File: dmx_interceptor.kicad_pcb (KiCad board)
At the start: 4 copper layers, 86 x 53 mm, 8 parts, among them J1 TB010-508-02BE, J2 TB010-508-02BE, J3 TB004-508-03BE, J4 TB004-508-03BE, U1 ARDUINO_PRO_MINI

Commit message: output files for ordering & pcb fix
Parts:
- R1: footprint mart_library:smd_0603_1608-Metric -> dmx_interceptor:smd_0603_1608-Metric
- mod1, mod2: footprint mart_library:max485_to_rs485 -> dmx_interceptor:max485_to_rs485
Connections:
- U1 pad JP1_4: unconnected-(U1-VCC-PadJP1_4) -> /5V
- U1 pad JP6_1: unconnected-(U1-RAW-PadJP6_1) -> /VIN
- U1 pad JP7_1: unconnected-(U1-D9-PadJP7_1) -> /switch
- U1 pad JP7_11: unconnected-(U1-RXI_2-PadJP7_11) -> /D_RX
- U1 pad JP7_12: unconnected-(U1-TXO_2-PadJP7_12) -> /D_TX
- U1 pad JP7_4: unconnected-(U1-D6-PadJP7_4) -> /RE_DE_RX
- U1 pad JP7_5: unconnected-(U1-D5-PadJP7_5) -> /RE_DE_TX
- U1 pad JP7_9: unconnected-(U1-GND_2-PadJP7_9) -> GND
- mod1 pad 5: (no net) -> unconnected-(mod1-RO-Pad5)
- mod2 pad 8: (no net) -> unconnected-(mod2-DI-Pad8)
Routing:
- net unconnected-(U1-RAW-PadJP6_1): track 6.69 -> 0.00 mm
- net /VIN: track 0.00 -> 6.69 mm
- net unconnected-(U1-RST_2-PadJP7_10): vias 1 -> 0
- net unconnected-(U1-D10-PadJP6_12): vias 1 -> 0
- net GND: vias 1 -> 86
- net (no net): vias 86 -> 0
- removed copper zone on F.Cu, net (none)
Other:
- board text added: "RX A/3/+"
- board text added: "RX B/2/-"
- board text added: "RX GND/1"
- board text added: "TX A/3/+"
- board text added: "TX B/2/-"
- board text added: "TX GND/1"
- board text added: "V1.1 - Mart Haarman - MHWD.NL"
- board text removed: "RX (A)(3)(+)"
- board text removed: "RX (B)(2)(-)"
- board text removed: "RX GND (1)"
- board text removed: "TX (A)(3)(+)"
- board text removed: "TX (B)(2)(-)"
- board text removed: "TX GND (1)"
- board text removed: "V1 - Mart Haarman - MHWD.NL"

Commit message: change resistor to throughole
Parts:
- R1: footprint dmx_interceptor:smd_0603_1608-Metric -> dmx_interceptor:R_THT
- moved R1 16.3 mm to (66.0, 105.9), turned to 90 degrees
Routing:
- net /switch: track 33.6 -> 35.3 mm
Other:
- board text added: "V1.2 - Mart Haarman - MHWD.NL"
- board text removed: "V1.1 - Mart Haarman - MHWD.NL"

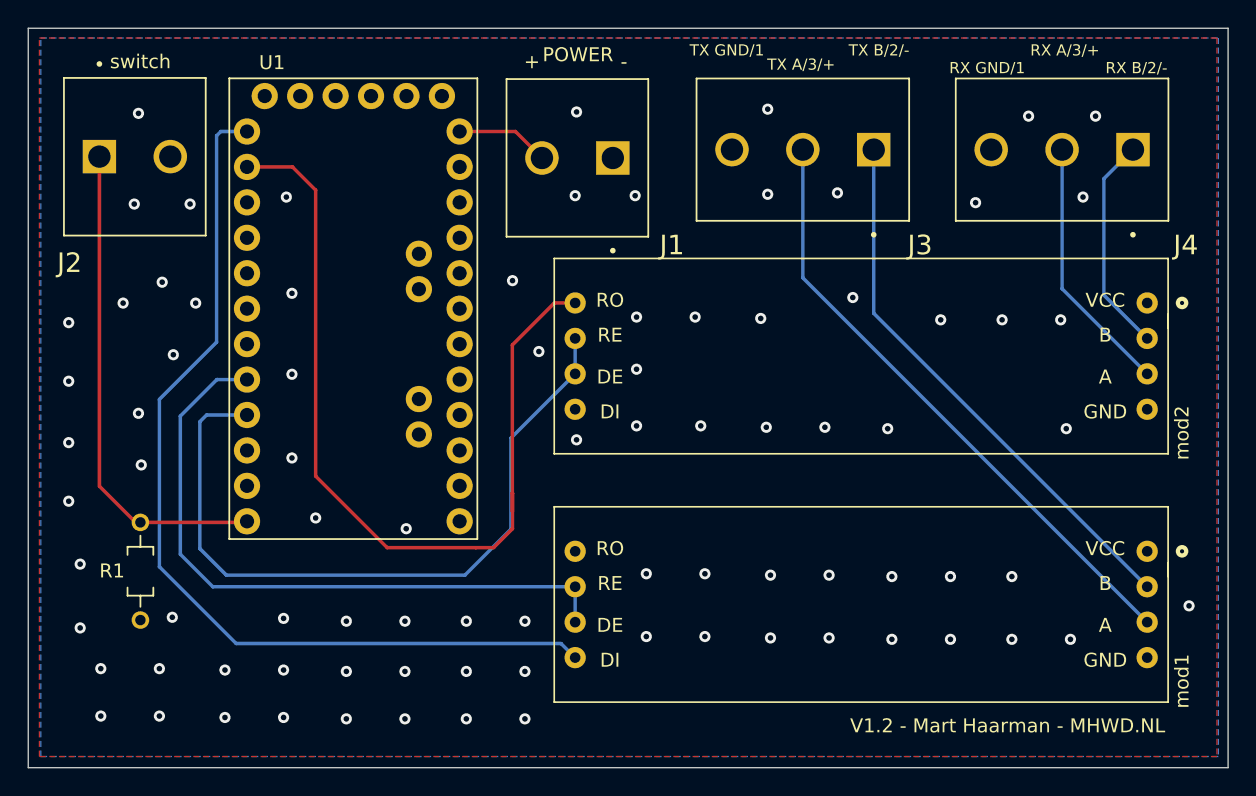
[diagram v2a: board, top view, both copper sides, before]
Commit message: added 4 mounting holes
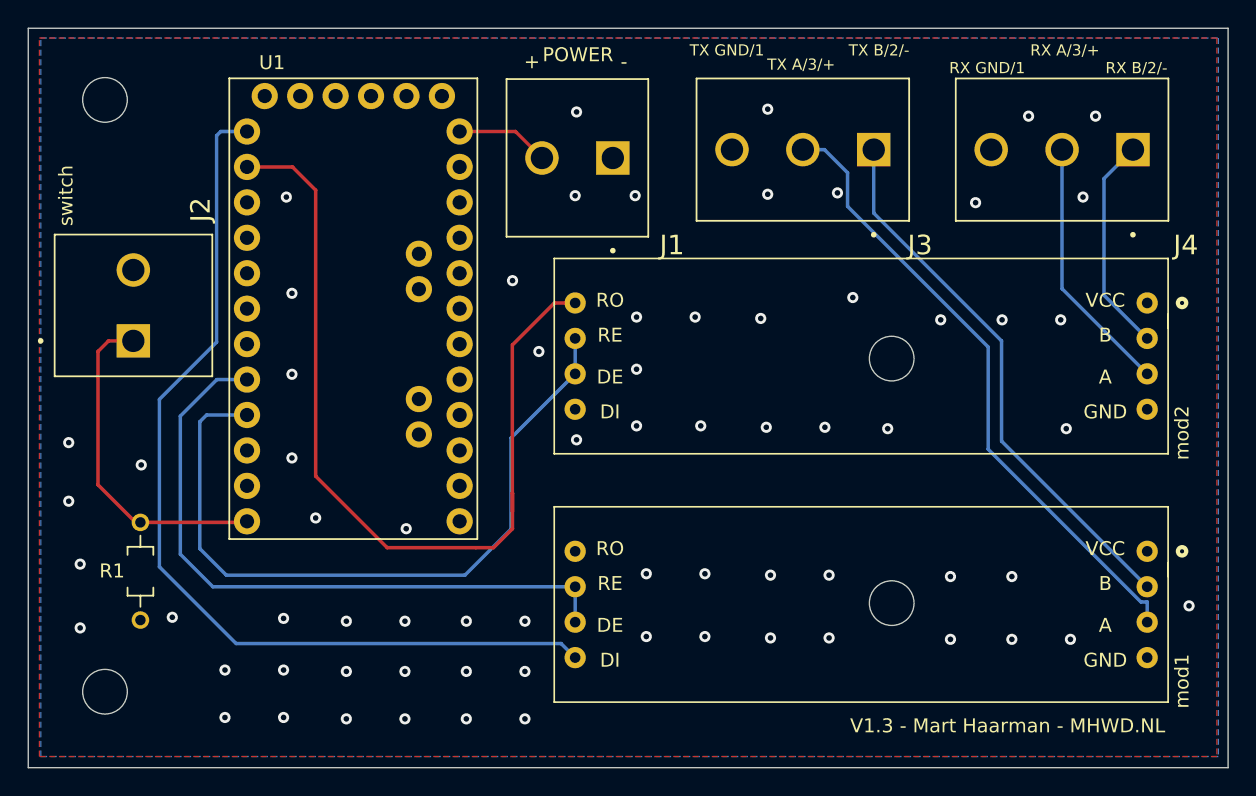
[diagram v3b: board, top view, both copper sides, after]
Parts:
- added REF**: MountingHole_3.2mm_M3, MountingHole:MountingHole_3.2mm_M3, F.Cu at (63.5, 114.6)
- added REF**: MountingHole_3.2mm_M3, MountingHole:MountingHole_3.2mm_M3, F.Cu at (119.9, 108.2)
- added REF**: MountingHole_3.2mm_M3, MountingHole:MountingHole_3.2mm_M3, F.Cu at (119.9, 90.7)
- added REF**: MountingHole_3.2mm_M3, MountingHole:MountingHole_3.2mm_M3, F.Cu at (63.5, 72.1)
- moved J2 13.4 mm to (65.5, 89.4), turned to 90 degrees
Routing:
- net /switch: track 35.3 -> 24.3 mm
- net /TX-(A)DATA+(3): track 44.1 -> 45.3 mm
- net GND: vias 86 -> 70
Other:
- board text added: "V1.3 - Mart Haarman - MHWD.NL"
- board text removed: "V1.2 - Mart Haarman - MHWD.NL"
